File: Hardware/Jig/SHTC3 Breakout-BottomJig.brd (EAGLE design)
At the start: 25.4 x 25.4 mm, 33 parts, among them J3 PTH, U1 SHTC3

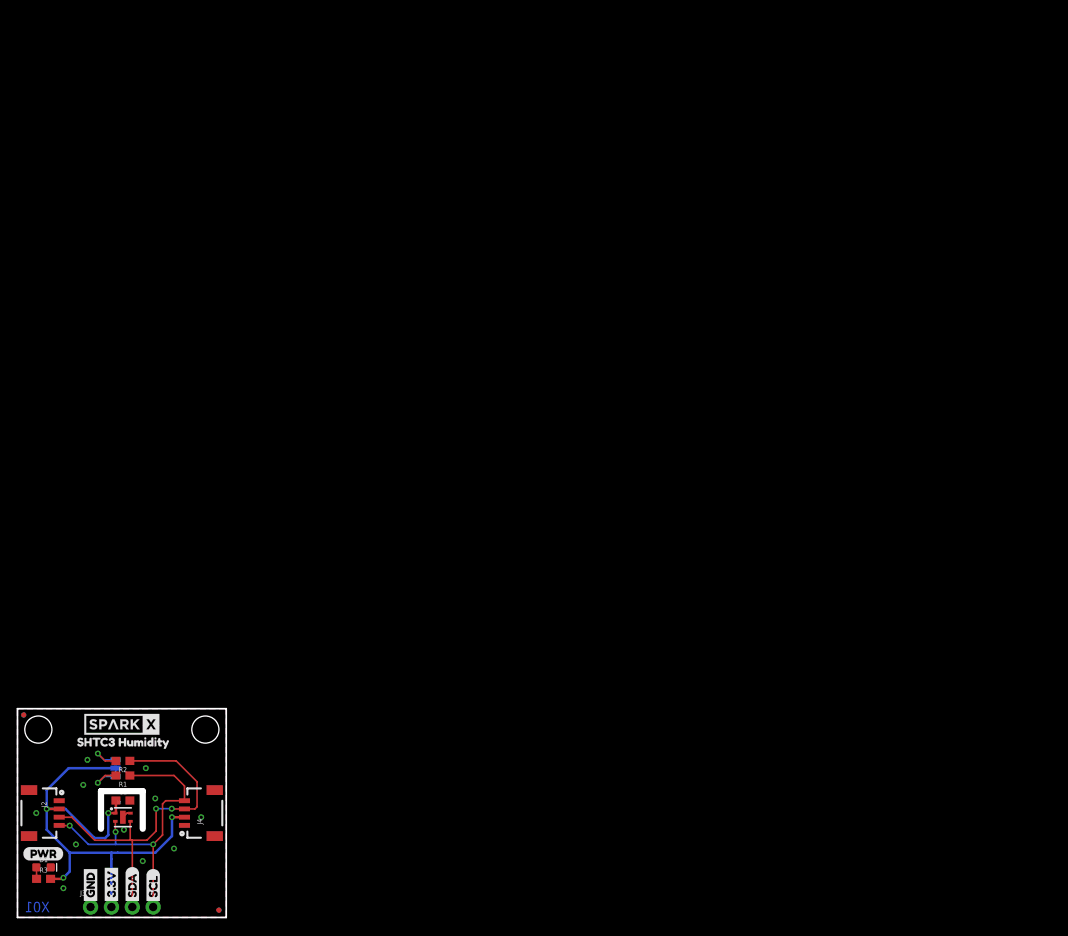
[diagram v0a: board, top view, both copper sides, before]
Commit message: Correcting HW Version
Looks like release version wasn't commited.  Updating.
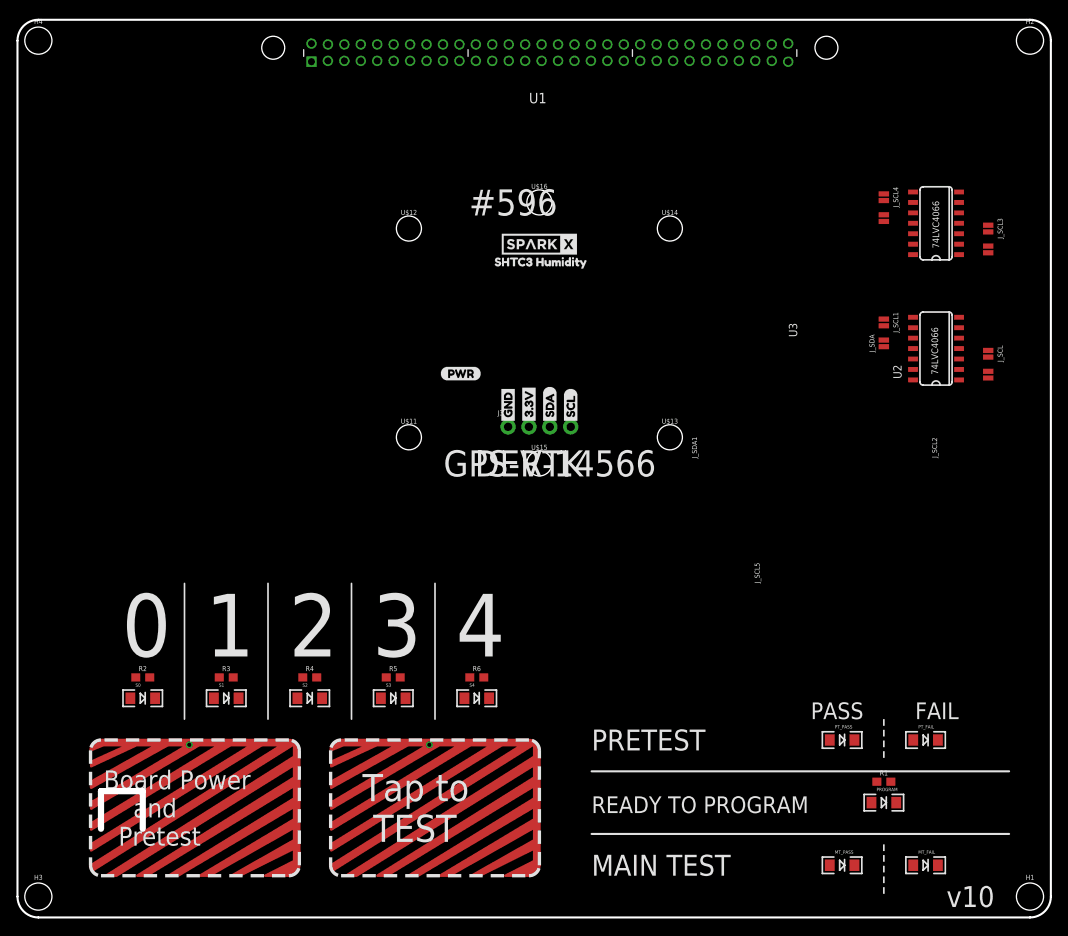
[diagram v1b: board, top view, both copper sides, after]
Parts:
- removed C1: 0.1uF, SparkFun-Capacitors:0603
- removed D1: RED, SparkFun-LED:LED-0603
- removed J2, J4: (no value), SparkFun-Connectors:1X04_1MM_RA
- removed JP1, JP2, JP5, JP6: FIDUCIALUFIDUCIAL, SparkFun:MICRO-FIDUCIAL
- removed JP3, JP4: STAND-OFF, SparkFun:STAND-OFF
- removed JP7: JUMPER-SMT_3_2-NC_TRACE_SILK, SparkFun-Jumpers:SMT-JUMPER_3_2-NC_TRACE_SILK
- added BUTTON1, BUTTON2: CAPSENSE_BUTTON_PAD_ONLY, Testing:CAPSENSE_BUTTON_PADS_ONLY
- added FRAME2: FRAME-LEDGER, SparkFun-Aesthetics:CREATIVE_COMMONS
- added H1, H2, H3, H4: STAND-OFF, SparkFun-Hardware:STAND-OFF
- added J_SCL, J_SCL3, J_SDA, J_SDA1: JUMPER-SMT_2_NO_NO-SILK, SparkFun-Jumpers:SMT-JUMPER_2_NO_NO-SILK
- added J_SCL1, J_SCL2, J_SCL4, J_SCL5: (no value), SparkFun-Jumpers:SMT-JUMPER_2_NO_NO-SILK
- added MT_FAIL, MT_PASS, PROGRAM, PT_FAIL, PT_PASS, S0, S1, S2, S3, S4: (no value), Testing:LED-1206
- added R4, R5, R6: 330, SparkFun-Resistors:0603
- added U$11, U$12, U$13, U$14, U$15, U$16: (no value), SparkFun-Hardware:STAND-OFF-TIGHT
- added U2, U3: 74LVC4066, Testing:SO14
- R1, R2: value 2.2k -> 330
- R3: value 1k -> 330
- U1: value SHTC3 -> FLYING_JALAPENO; device SHTC3:SHTC3 -> Testing:FLYING_JALAPENO_V3_M
- moved U1 110.1 mm to (64.8, 109.2)
- moved R1 92.6 mm to (105.4, 16.5), turned to 0 degrees
- moved J3 77.4 mm to (59.7, 59.7)
- moved LOGO1 77.4 mm to (53.3, 62.2)
- moved U$1 77.4 mm to (63.5, 81.9)
- moved U$10 77.4 mm to (51.4, 66.2)
- moved U$2 77.4 mm to (63.5, 81.9)
- moved U$21 77.4 mm to (62.2, 59.9)
- moved U$22 77.4 mm to (59.7, 59.9)
- moved U$26 77.4 mm to (67.3, 59.9)
- moved U$27 77.4 mm to (64.8, 59.9)
- moved U$29 77.4 mm to (72.4, 62.7)
- moved U$3 77.4 mm to (59.7, 59.9)
- moved U$4 77.4 mm to (62.2, 59.9)
- moved U$5 77.4 mm to (64.8, 59.9)
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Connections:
- removed net N$1: JP7.3, R1.2
- removed net N$2: JP7.1, R2.2
- removed net N$3: D1.A, R3.1
- new net 3.3V_POWER: U1.2, U1.32, U2.14, U3.14
- new net 5V_POWER: U1.3, U1.33
- new net JALAPENO_CS: J_SDA1.1, U1.60, U3.11
- new net JALAPENO_I2C_EN: U1.24, U2.13, U2.5
- new net JALAPENO_MISO: J_SCL5.1, U1.29, U3.1
- new net JALAPENO_MOSI: J_SCL3.1, U1.59, U3.4
- new net JALAPENO_RX1-I: J_SDA.1, U1.52, U2.11
- new net JALAPENO_SCK: J_SCL4.1, U1.30, U3.8
- new net JALAPENO_SCL: J_SCL.1, U1.53, U2.4
- new net JALAPENO_SDA: J_SCL2.1, U1.23, U2.1
- new net JALAPENO_SERIAL_EN: U1.54, U2.12, U2.6
- new net JALAPENO_SPI_EN: U3.12, U3.13, U3.5, U3.6
- new net JALAPENO_TX1-O: J_SCL1.1, U1.22, U2.8
- new net J_24: U1.25
- new net J_25: U1.55
- new net J_26: U1.26
- new net J_27: U1.56
- new net J_28: U1.27
- new net J_29: U1.57
- new net J_30: U1.28
- new net J_A0: U1.37
- new net J_A1: U1.8
- new net J_A2: U1.38
- new net J_A3: U1.9
- new net J_A4: U1.39
- new net J_PWM2: U1.14
- new net J_PWM3: U1.44
- new net J_PWM4: U1.15
- new net J_PWM5: U1.45
- new net N$10: R6.2, U1.46
- new net N$11: R1.2, U1.19
- new net N$12: PROGRAM.A, R1.1
- new net N$13: R5.2, U1.17
- new net N$14: R4.2, U1.47
- new net N$15: R3.2, U1.18
- new net N$16: R2.2, U1.48
- new net N$17: R6.1, S4.A
- new net N$18: R5.1, S3.A
- new net N$19: R4.1, S2.A
- new net N$20: R3.1, S1.A
- new net N$21: R2.1, S0.A
- new net N$4: PT_PASS.A, U1.7
- new net N$5: PT_FAIL.A, U1.36
- new net N$6: MT_PASS.A, U1.6
- new net N$7: MT_FAIL.A, U1.35
- new net N$8: BUTTON2.CAPSENSE_PAD, U1.58
- new net N$9: BUTTON1.CAPSENSE_PAD, U1.5
- new net TARGET_CS: J_SDA1.2, U3.10
- new net TARGET_MISO: J_SCL5.2, U3.2
- new net TARGET_MOSI: J_SCL3.2, U3.3
- new net TARGET_RX: J_SCL1.2, U2.9
- new net TARGET_SCK: J_SCL4.2, U3.9
- new net TARGET_SCL: J_SCL.2, U2.3
- new net TARGET_SDA: J_SCL2.2, U2.2
- new net TARGET_TX: J_SDA.2, U2.10
- net 3.3V: no longer C1.1, J2.2, J4.2, JP7.2, R3.2, U1.1
- net GND: now also MT_FAIL.C, MT_PASS.C, PROGRAM.C, PT_FAIL.C, PT_PASS.C, S0.C, S1.C, S2.C, S3.C, S4.C, U1.1, U1.31, U2.7, U3.7; no longer C1.2, D1.C, J2.1, J4.1, U1.4, U1.5
- net SCL: no longer J2.4, J4.4, R1.1, U1.2
- net SDA: no longer J2.3, J4.3, R2.1, U1.3
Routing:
- net 3.3V: track 62.7 -> 0.00 mm, vias 4 -> 0
- net SDA: track 43.9 -> 0.00 mm, vias 2 -> 0
- net SCL: track 40.0 -> 0.00 mm, vias 3 -> 0
- net N$2: track 5.04 -> 0.00 mm, vias 1 -> 0
- net N$1: track 5.04 -> 0.00 mm, vias 1 -> 0
- net N$3: track 1.41 -> 0.00 mm
- net GND: track 1.13 -> 0.00 mm, vias 11 -> 0
- removed copper zone on layer 1, net GND
- removed copper zone on layer 16, net GND
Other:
- board size 25.4 x 25.4 mm -> 125.7 x 109.2 mm
- board text added: "#596"
- board text added: "0"
- board text added: "1"
- board text added: "2"
- board text added: "3"
- board text added: "4"
- board text added: "Board Power and Pretest"
- board text added: "DEV-14566"
- board text added: "FAIL"
- board text added: "GPS-RTK"
- board text added: "MAIN TEST"
- board text added: "PASS"
- board text added: "PRETEST"
- board text added: "READY TO PROGRAM"
- board text added: "Tap to TEST"
- board text added: "v10"
- board text removed: "X01"
